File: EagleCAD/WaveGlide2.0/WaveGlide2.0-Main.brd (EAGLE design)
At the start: 80 x 100 mm, 58 parts, among them CN3 0, IC1 MC33502D, K2 MS-20-310-HN, Q2 reset, U1 ATMEGA328P_TQFP, U2 BMP180, U3 MPXV7002, U4 TPS55340PWP, U5 UG-2828GDEDF11, U6 TPS61222DCKR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

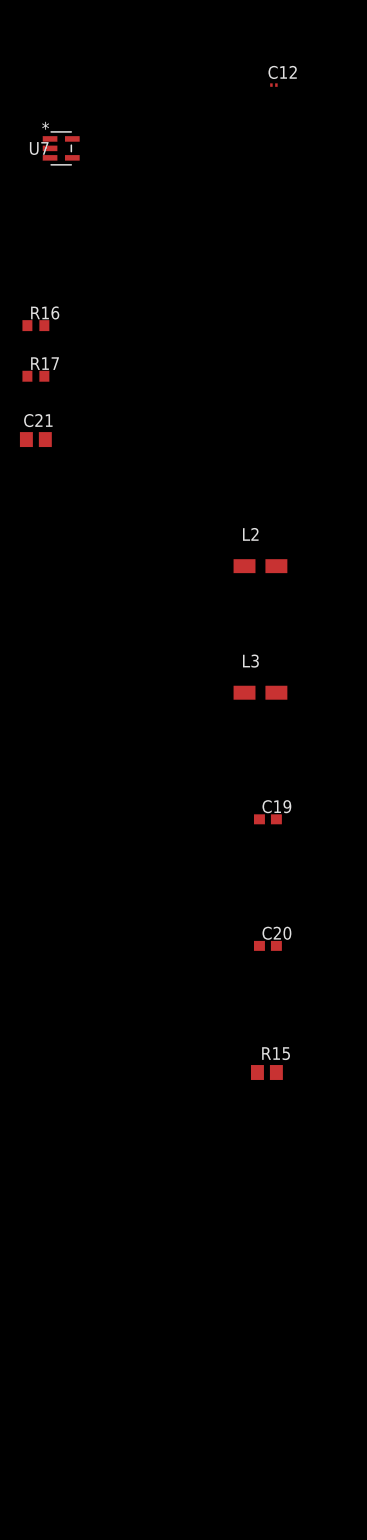
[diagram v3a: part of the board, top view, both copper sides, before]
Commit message: Add 3V3 Regulator
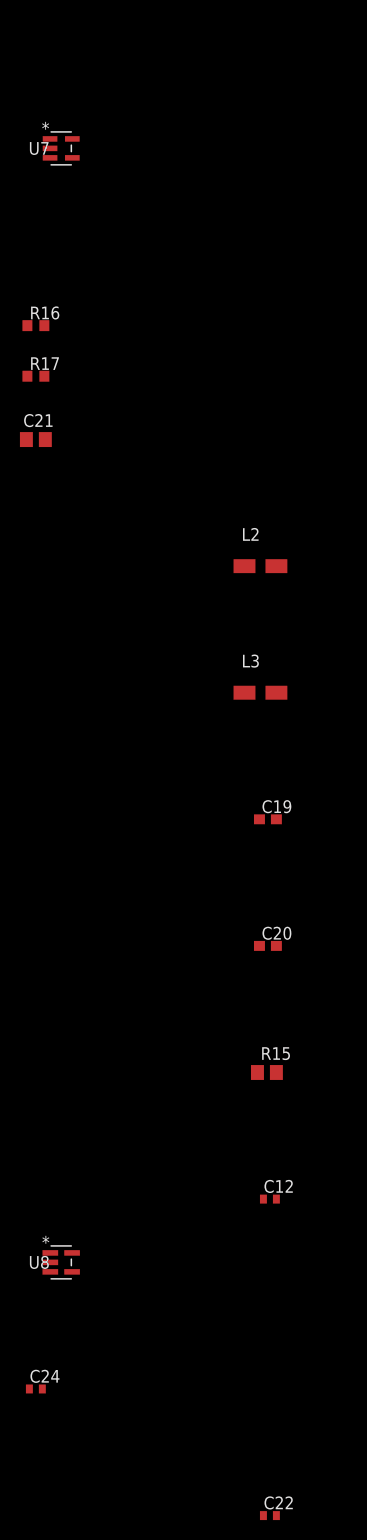
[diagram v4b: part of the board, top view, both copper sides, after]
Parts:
- added C22: 10nF, resistor:C0402
- added C24: 2.2uF, resistor:C0402
- added U8: TPS79933DDCR, CustomParts:DDC5
- C12: device resistor:C0201 -> resistor:C0402
- moved C12 111.8 mm to (-0.65, -243.8)
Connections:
- new net N$11: C22.1, U8.4
- net GND: now also C22.2, C24.2, U8.2
- net SYS_3V3: now also C24.1, U8.5
- net SYS_5V: now also U8.1, U8.3
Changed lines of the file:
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@@
 <attribute name="POPULATE" value="1" x="-7.62" y="-11.43" size="1.778" layer="27" display="off"/>
 </element>
-<element name="C12" library="resistor" library_urn="urn:adsk.eagle:library:348" package="C0201" package3d_urn="urn:adsk.eagle:package:26209/1" value="22nF" x="-0.25" y="-132.08">
-<attribute name="MPN" value="GRM033R60J223KE01D" x="-0.25" y="-132.08" size="1.778" layer="27" display="off"/>
-<attribute name="POPULATE" value="1" x="-0.25" y="-132.08" size="1.778" layer="27" display="off"/>
+<element name="C12" library="resistor" library_urn="urn:adsk.eagle:library:348" package="C0402" package3d_urn="urn:adsk.eagle:package:26136/1" value="22nF" x="-0.65" y="-243.84">
+<attribute name="MPN" value="GRM155R60J223KA01D" x="-0.65" y="-243.84" size="1.778" layer="27" display="off"/>
+<attribute name="POPULATE" value="1" x="-0.65" y="-243.84" size="1.778" layer="27" display="off"/>
+<attribute name="TOL" value="10%" x="-0.65" y="-243.84" size="1.778" layer="27" display="off"/>
+<attribute name="VOLT" value="6.3V" x="-0.65" y="-243.84" size="1.778" layer="27" display="off"/>
 </element>
 <element name="C13" library="resistor" library_urn="urn:adsk.eagle:library:348" package="C0805" package3d_urn="urn:adsk.eagle:package:26137/1" value="10nF" x="-7.62" y="-24.13">
@@
 <attribute name="POPULATE" value="1" x="-1.6" y="-193.04" size="0.8" layer="27" ratio="14" display="off"/>
 <attribute name="TOL" value="20%" x="-1.6" y="-193.04" size="1.778" layer="27" display="off"/>
+</element>
+<element name="U8" library="CustomParts" library_urn="urn:adsk.eagle:library:2193978" package="DDC5" package3d_urn="urn:adsk.eagle:package:2443411/1" value="TPS79933DDCR" x="-21.59" y="-250.19">
+<attribute name="MANUFACTURER_PART_NUMBER" value="TPS79933DDCR" x="-21.59" y="-250.19" size="0.8" layer="27" ratio="14" display="off"/>
+<attribute name="VENDOR" value="Texas Instruments" x="-21.59" y="-250.19" size="0.8" layer="27" ratio="14" display="off"/>
+</element>
+<element name="C22" library="resistor" library_urn="urn:adsk.eagle:library:348" package="C0402" package3d_urn="urn:adsk.eagle:package:26136/1" value="10nF" x="-0.65" y="-275.59">
+<attribute name="MPN" value="GRM033R70J103KA01D" x="-0.65" y="-275.59" size="1.778" layer="27" display="off"/>
+<attribute name="POPULATE" value="1" x="-0.65" y="-275.59" size="1.778" layer="27" display="off"/>
+<attribute name="TOL" value="10%" x="-0.65" y="-275.59" size="1.778" layer="27" display="off"/>
+<attribute name="VOLT" value="6.3V" x="-0.65" y="-275.59" size="1.778" layer="27" display="off"/>
+</element>
+<element name="C24" library="resistor" library_urn="urn:adsk.eagle:library:348" package="C0402" package3d_urn="urn:adsk.eagle:package:26136/1" value="2.2uF" x="-24.13" y="-262.89">
+<attribute name="MPN" value="
+JMK105BJ225MV-F" x="-24.13" y="-262.89" size="1.778" layer="27" display="off"/>
+<attribute name="POPULATE" value="1" x="-24.13" y="-262.89" size="1.778" layer="27" display="off"/>
+<attribute name="TOL" value="20%" x="-24.13" y="-262.89" size="1.778" layer="27" display="off"/>
+<attribute name="VOLT" value="6.3V" x="-24.13" y="-262.89" size="1.778" layer="27" display="off"/>
 </element>
 </elements>
@@
 <contactref element="U7" pad="2"/>
 <contactref element="C19" pad="2"/>
+<contactref element="U8" pad="2"/>
+<contactref element="C22" pad="2"/>
+<contactref element="C24" pad="2"/>
+<wire x1="0" y1="-231.14" x2="0" y2="-243.84" width="0" layer="19" extent="1-1"/>
+<wire x1="-22.6822" y1="-250.19" x2="0" y2="-243.84" width="0" layer="19" extent="1-1"/>
+<wire x1="0" y1="-275.59" x2="-22.6822" y2="-250.19" width="0" layer="19" extent="1-1"/>
+<wire x1="-23.48" y1="-262.89" x2="0" y2="-275.59" width="0" layer="19" extent="1-1"/>
+<wire x1="0" y1="-205.74" x2="0" y2="-231.14" width="0" layer="19" extent="1-1"/>
+<wire x1="-23.18" y1="-167.64" x2="0" y2="-205.74" width="0" layer="19" extent="1-1"/>
 <wire x1="-23.28" y1="-161.29" x2="-23.18" y2="-167.64" width="0" layer="19" extent="1-1"/>
-<wire x1="0" y1="-205.74" x2="-23.28" y2="-161.29" width="0" layer="19" extent="1-1"/>
-<wire x1="-22.7076" y1="-138.43" x2="0" y2="-205.74" width="0" layer="19" extent="1-1"/>
+<wire x1="-22.7076" y1="-138.43" x2="-23.28" y2="-161.29" width="0" layer="19" extent="1-1"/>
 <wire x1="-23.18" y1="-119.38" x2="-22.7076" y2="-138.43" width="0" layer="19" extent="1-1"/>
 <wire x1="-23.18" y1="-113.03" x2="-23.18" y2="-119.38" width="0" layer="19" extent="1-1"/>
@@
 <wire x1="0" y1="-99.740034375" x2="0" y2="-100.390046875" width="0" layer="19" extent="1-1"/>
 <wire x1="0" y1="-76.2" x2="0" y2="-99.740034375" width="0" layer="19" extent="1-1"/>
-<wire x1="0" y1="-231.14" x2="0" y2="-76.2" width="0" layer="19" extent="1-1"/>
-<wire x1="-8.47" y1="-48.26" x2="0" y2="-231.14" width="0" layer="19" extent="1-1"/>
+<wire x1="-8.47" y1="-48.26" x2="0" y2="-76.2" width="0" layer="19" extent="1-1"/>
 <wire x1="-6.67" y1="-43.18" x2="-8.47" y2="-48.26" width="0" layer="19" extent="1-1"/>
 <wire x1="-6.67" y1="-36.83" x2="-6.67" y2="-43.18" width="0" layer="19" extent="1-1"/>
@@
 <wire x1="-6.67" y1="-11.43" x2="-6.67" y2="-24.13" width="0" layer="19" extent="1-1"/>
 <wire x1="-6.67" y1="-5.08" x2="-6.67" y2="-11.43" width="0" layer="19" extent="1-1"/>
-<wire x1="0" y1="-132.08" x2="-22.7076" y2="-138.43" width="0" layer="19" extent="1-1"/>
 <wire x1="35.3" y1="31" x2="-6.67" y2="-5.08" width="0" layer="19" extent="1-1"/>
 <wire x1="40" y1="26.25" x2="35.3" y2="31" width="0" layer="19" extent="1-1"/>
@@
 <contactref element="U1" pad="6"/>
 <contactref element="U1" pad="18"/>
+<contactref element="U8" pad="5"/>
+<contactref element="C24" pad="1"/>
 <wire x1="34.25" y1="94.088" x2="45.75" y2="94.088" width="0" layer="19" extent="16-16"/>
 <wire x1="34.798" y1="89.728" x2="34.25" y2="94.088" width="0" layer="19" extent="16-16"/>
 <wire x1="32.258" y1="89.728" x2="34.798" y2="89.728" width="0" layer="19" extent="16-16"/>
 <wire x1="23.3426" y1="85.63" x2="32.258" y2="89.728" width="0" layer="19" extent="1-16"/>
+<wire x1="20.32" y1="77.842" x2="23.3426" y2="85.63" width="0" layer="19" extent="1-1"/>
 <wire x1="14.7574" y1="86.43" x2="23.3426" y2="85.63" width="0" layer="19" extent="1-1"/>
 <wire x1="14.7574" y1="88.03" x2="14.7574" y2="86.43" width="0" layer="19" extent="1-1"/>
@@
 <wire x1="15.24" y1="97.37" x2="10.92" y2="94.06" width="0" layer="19" extent="1-1"/>
 <wire x1="18.034" y1="97.37" x2="15.24" y2="97.37" width="0" layer="19" extent="1-1"/>
+<wire x1="20.955" y1="97.37" x2="18.034" y2="97.37" width="0" layer="19" extent="1-1"/>
 <wire x1="8.128" y1="83.654" x2="14.7574" y2="86.43" width="0" layer="19" extent="1-1"/>
-<wire x1="20.955" y1="97.37" x2="14.7574" y2="86.43" width="0" layer="19" extent="1-1"/>
-<wire x1="20.32" y1="77.842" x2="20.955" y2="97.37" width="0" layer="19" extent="1-1"/>
+<wire x1="-20.4978" y1="-249.24" x2="20.32" y2="77.842" width="0" layer="19" extent="1-1"/>
+<wire x1="-24.78" y1="-262.89" x2="-20.4978" y2="-249.24" width="0" layer="19" extent="1-1"/>
 </signal>
 <signal name="MCU_AREF">
@@
 <contactref element="C18" pad="1"/>
 <contactref element="U6" pad="2"/>
+<contactref element="U8" pad="1"/>
+<contactref element="U8" pad="3"/>
 <wire x1="-14.9479" y1="-107.95" x2="-25.08" y2="-119.38" width="0" layer="19" extent="1-1"/>
 <wire x1="-12.9921" y1="-108.6" x2="-14.9479" y2="-107.95" width="0" layer="19" extent="1-1"/>
+<wire x1="-22.6822" y1="-249.24" x2="-25.08" y2="-119.38" width="0" layer="19" extent="1-1"/>
+<wire x1="-22.6822" y1="-251.14" x2="-22.6822" y2="-249.24" width="0" layer="19" extent="1-1"/>
 <wire x1="29.15" y1="80.645" x2="-14.9479" y2="-107.95" width="0" layer="19" extent="1-1"/>
 <wire x1="47.31" y1="80.01" x2="29.15" y2="80.645" width="0" layer="19" extent="1-1"/>
@@
 <contactref element="C12" pad="1"/>
 <contactref element="U4" pad="5"/>
-<wire x1="-0.5" y1="-132.08" x2="-5.6388" y2="-102.34008125" width="0" layer="19" extent="1-1"/>
+<wire x1="-1.3" y1="-243.84" x2="-5.6388" y2="-102.34008125" width="0" layer="19" extent="1-1"/>
 </signal>
 <signal name="TPS55340_COMP">
@@
 <wire x1="-22.7076" y1="-137.48" x2="0" y2="-193.04" width="0" layer="19" extent="1-1"/>
 </signal>
+<signal name="N$11">
+<contactref element="U8" pad="4"/>
+<contactref element="C22" pad="1"/>
+<wire x1="-20.4978" y1="-251.14" x2="-1.3" y2="-275.59" width="0" layer="19" extent="1-1"/>
+</signal>
 </signals>

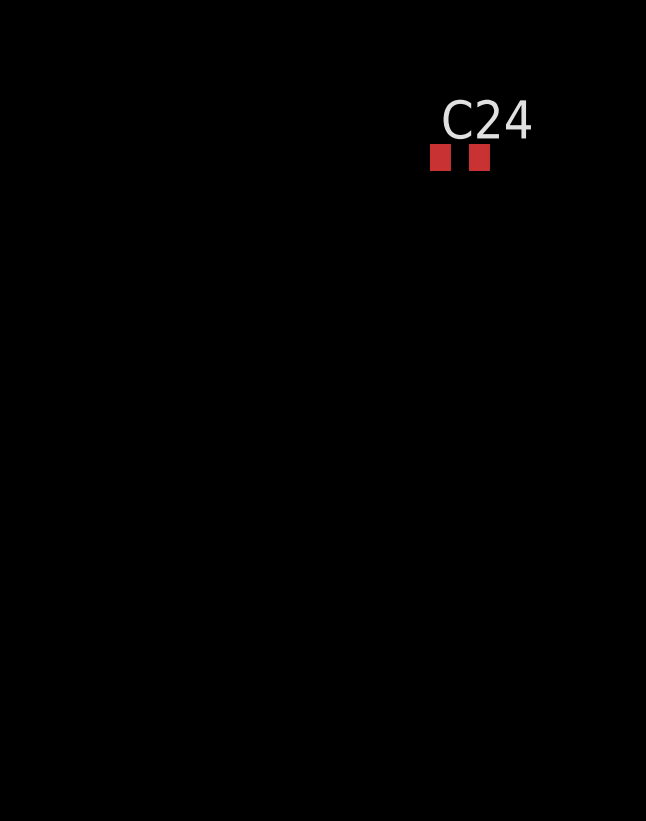
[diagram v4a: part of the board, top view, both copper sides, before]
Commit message: Add diodes to power regulators
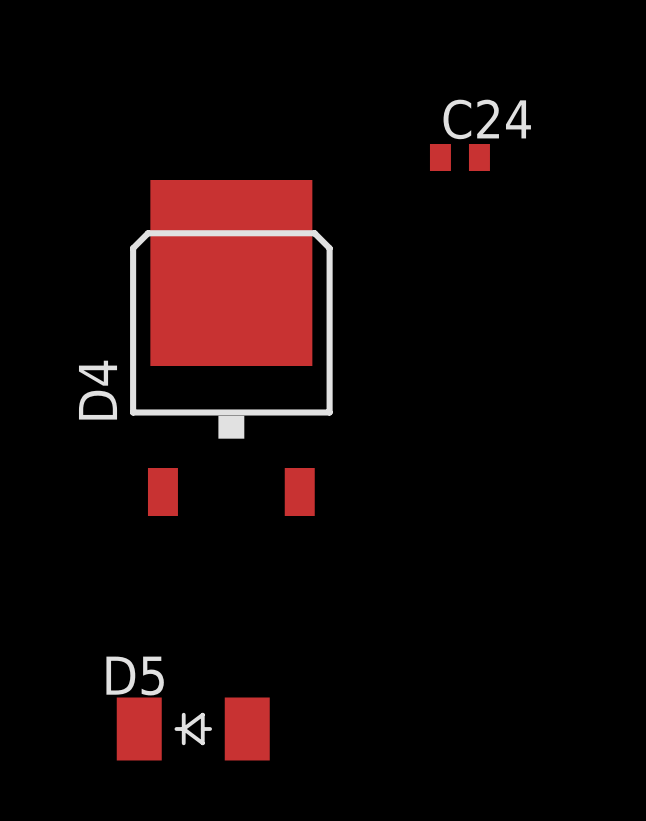
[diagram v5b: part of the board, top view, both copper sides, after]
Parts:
- added D4: SCHOTTKYDPAK, CustomParts:D-PAK_TO252AA
- added D5: SCHOTTKYSOT-123, CustomParts:SOD-123_MINI-SMA
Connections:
- net N$11 renamed TPS79933_NR
- net N$6 renamed TPS61222_L
- net N$5: now also D5.A
- net SOLENOID_12V: now also D4.4
- net SYS_13V: now also D5.C
- net TPS55340_SW: now also D4.1, D4.3
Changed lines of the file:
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@@
 <attribute name="VOLT" value="6.3V" x="-24.13" y="-262.89" size="1.778" layer="27" display="off"/>
 </element>
+<element name="D4" library="CustomParts" library_urn="urn:adsk.eagle:library:2193978" package="D-PAK_TO252AA" package3d_urn="urn:adsk.eagle:package:2443426/1" value="SCHOTTKYDPAK" x="-31.75" y="-269.24"/>
+<element name="D5" library="CustomParts" library_urn="urn:adsk.eagle:library:2193978" package="SOD-123_MINI-SMA" package3d_urn="urn:adsk.eagle:package:2443425/1" value="SCHOTTKYSOT-123" x="-33.02" y="-281.94"/>
 </elements>
 <signals>
@@
 <contactref element="C20" pad="1"/>
 <contactref element="C21" pad="1"/>
+<contactref element="D5" pad="C"/>
+<wire x1="-25.08" y1="-167.64" x2="-1.7" y2="-218.44" width="0" layer="19" extent="1-1"/>
 <wire x1="-24.98" y1="-156.21" x2="-25.08" y2="-167.64" width="0" layer="19" extent="1-1"/>
-<wire x1="-1.7" y1="-218.44" x2="-24.98" y2="-156.21" width="0" layer="19" extent="1-1"/>
-<wire x1="47.498" y1="91.628" x2="-1.7" y2="-218.44" width="0" layer="19" extent="1-16"/>
+<wire x1="-34.82" y1="-281.94" x2="-1.7" y2="-218.44" width="0" layer="19" extent="1-1"/>
+<wire x1="47.498" y1="91.628" x2="-24.98" y2="-156.21" width="0" layer="19" extent="1-16"/>
 <wire x1="46.75" y1="94.088" x2="47.498" y2="91.628" width="0" layer="19" extent="16-16"/>
 </signal>
@@
 <contactref element="C14" pad="1"/>
 <contactref element="C15" pad="1"/>
+<contactref element="D4" pad="4"/>
 <wire x1="-8.47" y1="-58.42" x2="-2.8" y2="-76.2" width="0" layer="19" extent="1-1"/>
 <wire x1="-8.57" y1="-36.83" x2="-8.47" y2="-58.42" width="0" layer="19" extent="1-1"/>
 <wire x1="44.7" y1="31" x2="-8.57" y2="-36.83" width="0" layer="19" extent="1-1"/>
 <wire x1="34.13" y1="42.95" x2="44.7" y2="31" width="0" layer="19" extent="1-1"/>
+<wire x1="-31.75" y1="-266.74" x2="-2.8" y2="-76.2" width="0" layer="19" extent="1-1"/>
 </signal>
 <signal name="MCU_I2C_SCL">
@@
 <contactref element="U4" pad="2"/>
 <contactref element="L1" pad="2"/>
+<contactref element="D4" pad="3"/>
+<contactref element="D4" pad="1"/>
 <wire x1="-5.6388" y1="-100.390046875" x2="-5.6388" y2="-99.740034375" width="0" layer="19" extent="1-1"/>
 <wire x1="-13.24" y1="-58.42" x2="-5.6388" y2="-99.740034375" width="0" layer="19" extent="1-1"/>
-</signal>
-<signal name="N$6">
+<wire x1="-29.47" y1="-274.04" x2="-5.6388" y2="-100.390046875" width="0" layer="19" extent="1-1"/>
+<wire x1="-34.03" y1="-274.04" x2="-29.47" y2="-274.04" width="0" layer="19" extent="1-1"/>
+</signal>
+<signal name="TPS61222_L">
 <contactref element="L2" pad="2"/>
 <contactref element="U6" pad="5"/>
@@
 <contactref element="L3" pad="2"/>
 <contactref element="U7" pad="1"/>
+<contactref element="D5" pad="A"/>
 <wire x1="-22.7076" y1="-137.48" x2="0" y2="-193.04" width="0" layer="19" extent="1-1"/>
-</signal>
-<signal name="N$11">
+<wire x1="-31.22" y1="-281.94" x2="0" y2="-193.04" width="0" layer="19" extent="1-1"/>
+</signal>
+<signal name="TPS79933_NR">
 <contactref element="U8" pad="4"/>
 <contactref element="C22" pad="1"/>

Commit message: Floor planning 12V regulator
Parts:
- moved D4 346.8 mm to (66.0, 63.5), turned to 270 degrees
- moved D5 341.0 mm to (29.2, 53.3), turned to 90 degrees
- moved C22 329.1 mm to (8.24, 53.3)
- moved C24 329.0 mm to (5.08, 64.8)
- moved C12 306.0 mm to (50.8, 57.8), turned to 270 degrees
- moved U8 298.7 mm to (8.89, 47.0)
- moved R15 293.3 mm to (60.5, 55.7), turned to 270 degrees
- moved C19 270.8 mm to (10.6, 64.8)
- moved L3 267.7 mm to (41.6, 71.1)
- moved C20 245.2 mm to (24.6, 25.4)
- moved L2 240.2 mm to (7.29, 59.7)
- moved C21 199.0 mm to (19.1, 26.7)
- moved R17 198.1 mm to (25.4, 30.5), turned to 180 degrees
- moved R16 196.8 mm to (25.4, 34.3)
- moved U7 177.4 mm to (19.1, 34.3), turned to 180 degrees
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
